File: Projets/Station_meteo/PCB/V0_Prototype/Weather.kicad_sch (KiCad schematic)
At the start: 0 parts

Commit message: Update PCB
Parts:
- added H1, H2, H3, H4: MountingHole_Pad, MountingHole:MountingHole_3.2mm_M3, symbol Mechanical:MountingHole_Pad
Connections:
- net GND: now also H1.1, H2.1, H3.1, H4.1
- no-connect marks 0 -> 6
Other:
- sheet Interfaces ports: added Direction, Water_Level; removed {I2C}

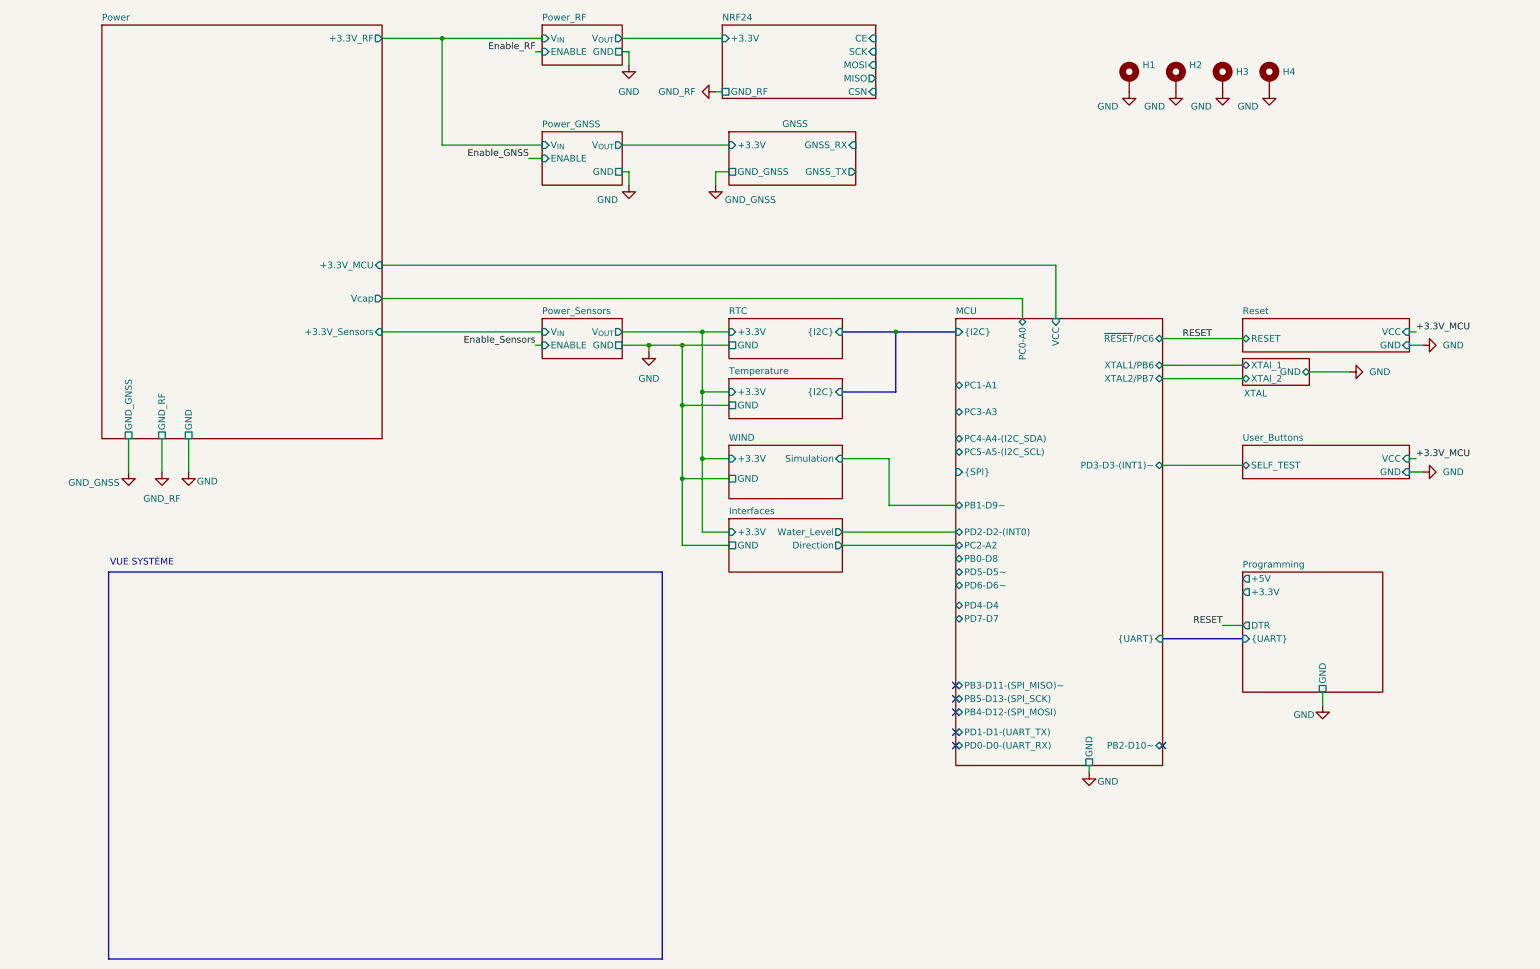
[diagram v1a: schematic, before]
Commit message: Add V1 THT version
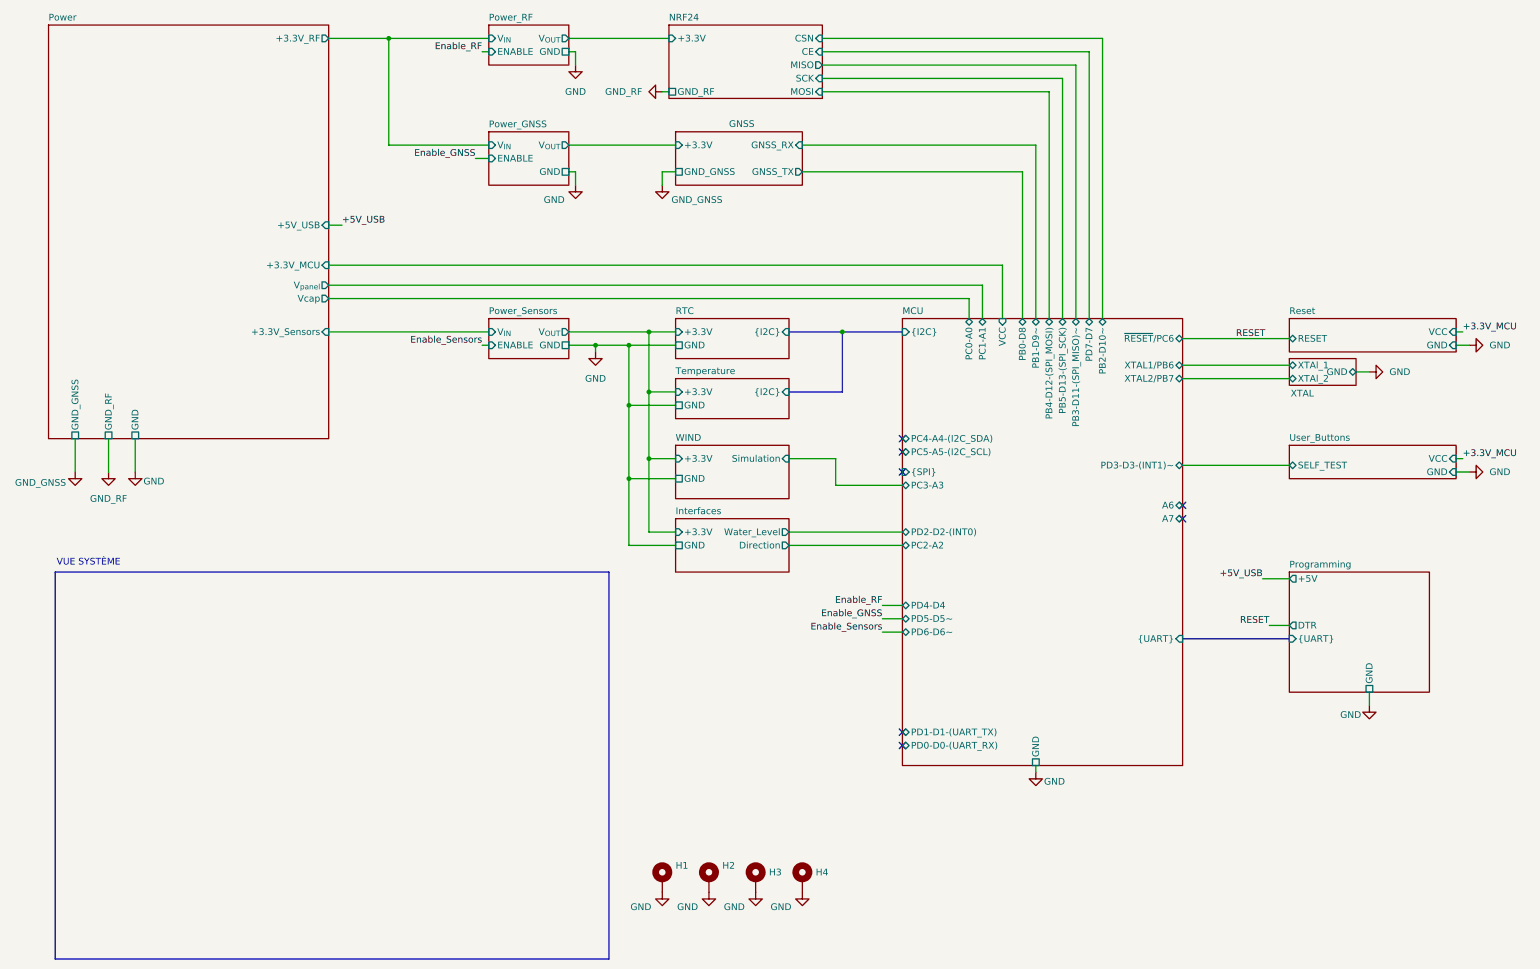
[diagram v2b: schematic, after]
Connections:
- no-connect marks 6 -> 7
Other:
- sheet MCU ports: added A6, A7; removed none
- sheet Power ports: added +5V_USB, V_{panel}; removed none
- sheet Programming ports: added none; removed +3.3V
- moved on the sheet: H1, H2, H3, H4
